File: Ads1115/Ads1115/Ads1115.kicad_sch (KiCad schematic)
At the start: 1 part, among them U1 ADS1115IDGS

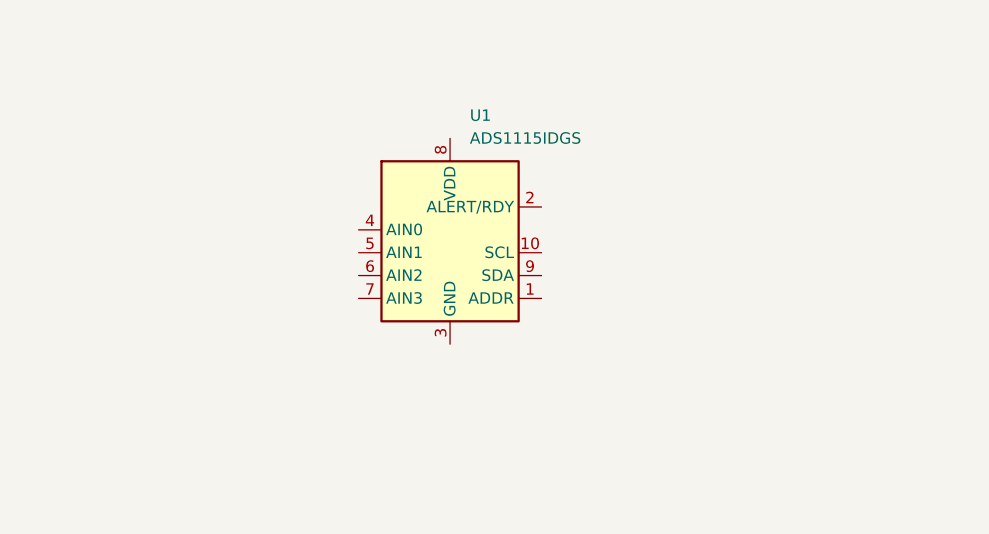
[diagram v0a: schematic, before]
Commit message: add ads1111 and ads1248
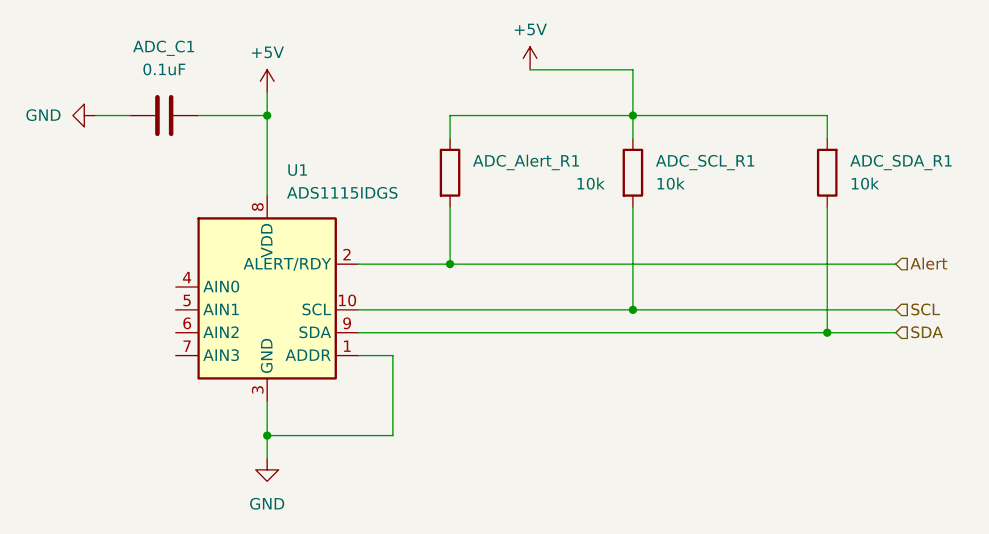
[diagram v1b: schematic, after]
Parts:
- added ADC_Alert_R1, ADC_SCL_R1, ADC_SDA_R1: 10k, Resistor_SMD:R_0402_1005Metric, symbol Device:R
- added ADC_C1: 0.1uF, Capacitor_SMD:C_0402_1005Metric, symbol Device:C
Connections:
- net GND: now reaches U1.1 (ADDR)
- net GND: now also U1.3 (GND), ADC_C1.1
- net SCL: now reaches U1.10 (SCL)
- net SCL: now also ADC_SCL_R1.2
- net Alert: now reaches U1.2 (ALERT/RDY)
- net Alert: now also ADC_Alert_R1.2
- net +5V: now reaches U1.8 (VDD)
- net +5V: now also ADC_Alert_R1.1, ADC_C1.2, ADC_SCL_R1.1, ADC_SDA_R1.2
- net SDA: now reaches U1.9 (SDA)
- net SDA: now also ADC_SDA_R1.1

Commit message: updates ads1115 and ads 1248
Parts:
- added ADC_C2, ADC_C3, ADC_C4, ADC_C5, ADC_C6, ADC_C7: 0.1uF, Capacitor_SMD:C_0402_1005Metric, symbol Device:C
- renumbered U1 to ADS1115_U1
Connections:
- net GND: now also ADC_C2.1, ADC_C3.1, ADC_C4.1, ADC_C5.1
- net A0: now reaches ADS1115_U1.4 (AIN0)
- net A0: now also ADC_C2.2, ADC_C6.2
- net A1: now reaches ADS1115_U1.5 (AIN1)
- net A1: now also ADC_C3.2, ADC_C6.1
- net A2: now reaches ADS1115_U1.6 (AIN2)
- net A2: now also ADC_C4.2, ADC_C7.1
- net A3: now reaches ADS1115_U1.7 (AIN3)
- net A3: now also ADC_C5.2, ADC_C7.2
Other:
- moved on the sheet: ADC_Alert_R1, ADC_SCL_R1, ADC_SDA_R1, ADS1115_U1
